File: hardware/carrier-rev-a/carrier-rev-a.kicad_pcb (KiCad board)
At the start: 2 copper layers, 250 x 210 mm, 107 parts, among them J1 SSQ-110-01-G-S, J10 SSQ-120-01-G-S, J11 SSQ-120-01-G-S, J2 SSQ-108-01-G-S, J3 SSQ-110-01-G-S, J4 SSQ-108-01-G-S, J5 SSQ-110-01-G-S, J6 SSQ-108-01-G-S, J7 SSQ-110-01-G-S, J8 SSQ-108-01-G-S, J9 5 V / 4 A INPUT, Q1 DMG2305UX-7, U2 TPS259470LRPWR, U3 AP2112K-3.3TRG1, U4 MCP23S17-E/SO, U5 SN74LVC8T245PWR, U6 SN74LVC8T245PWR, U7 SN74LVC1T45DBVR

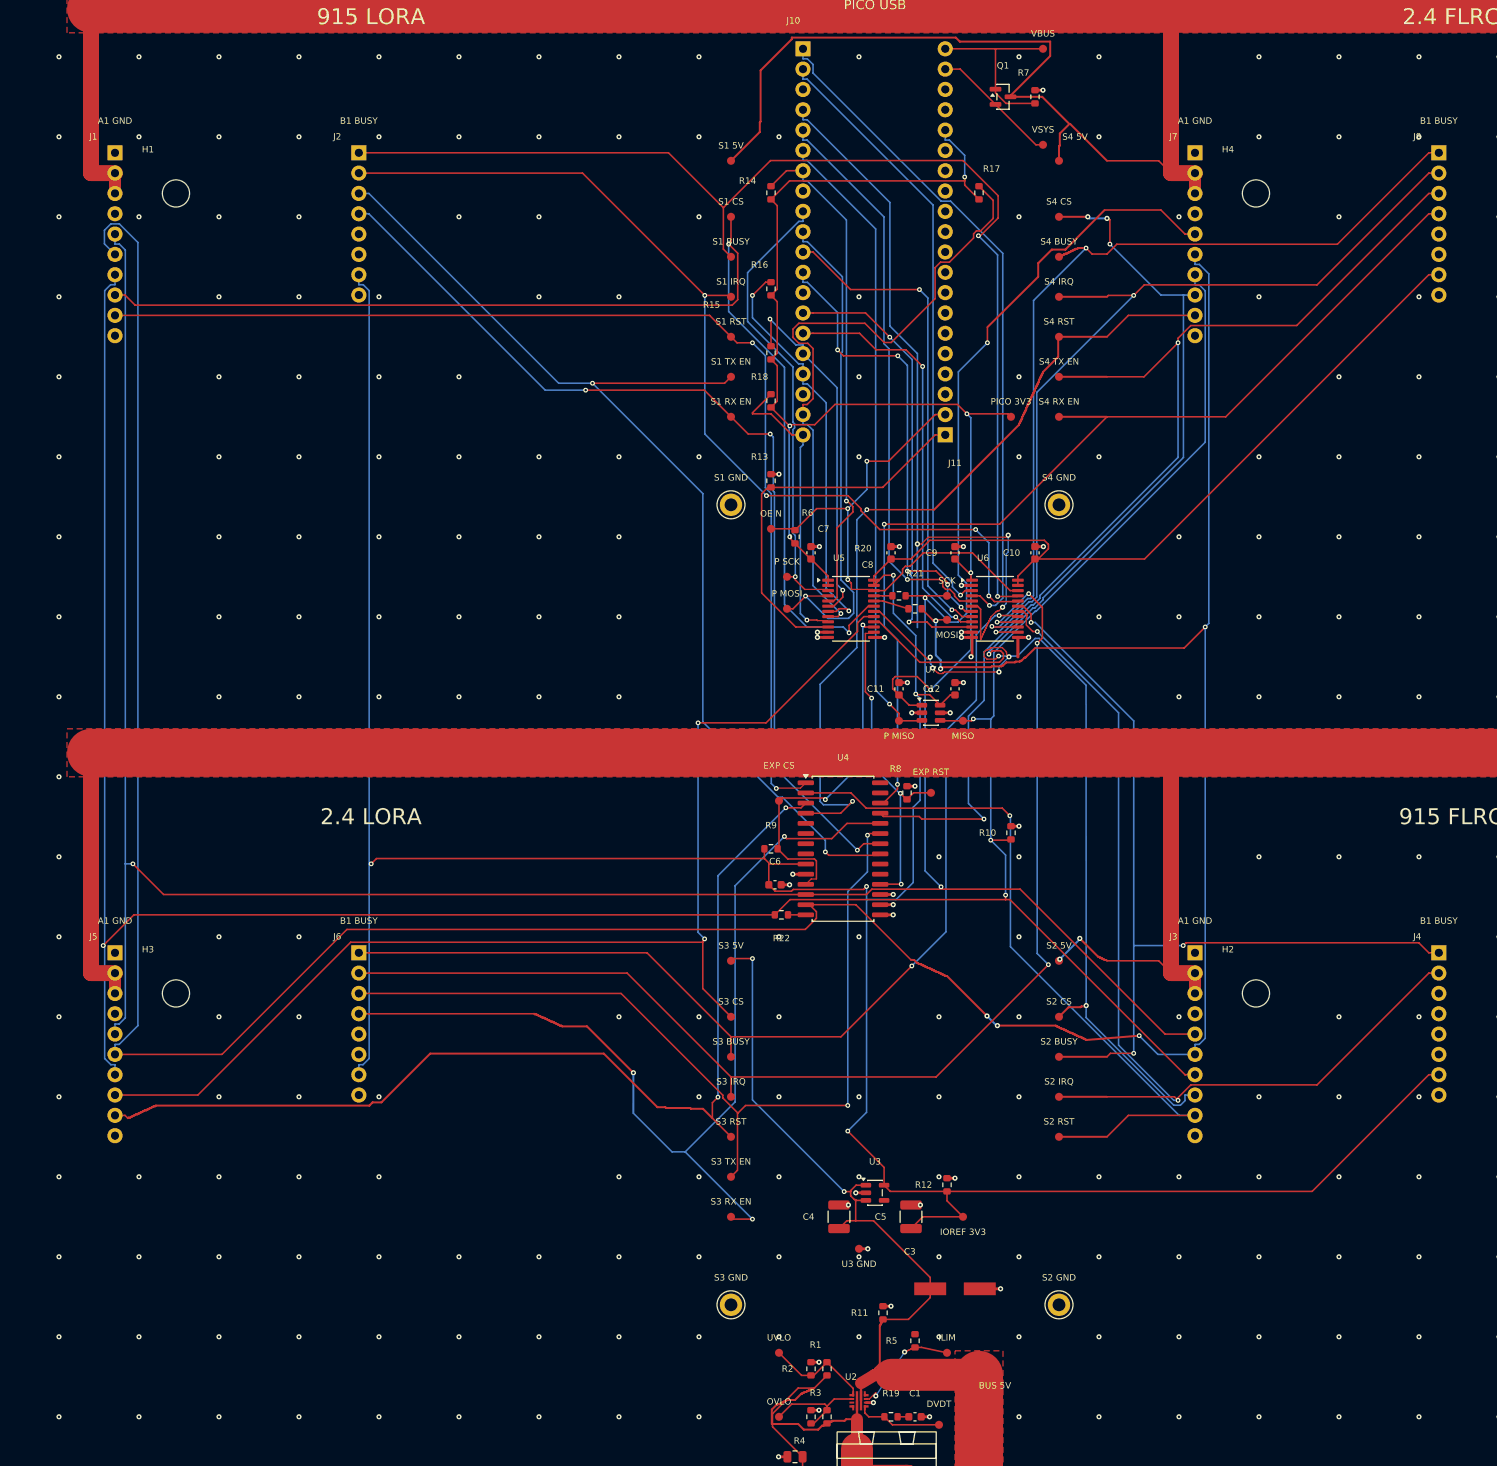
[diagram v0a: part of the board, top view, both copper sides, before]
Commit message: Improve Rev-A ground references and feedback routing
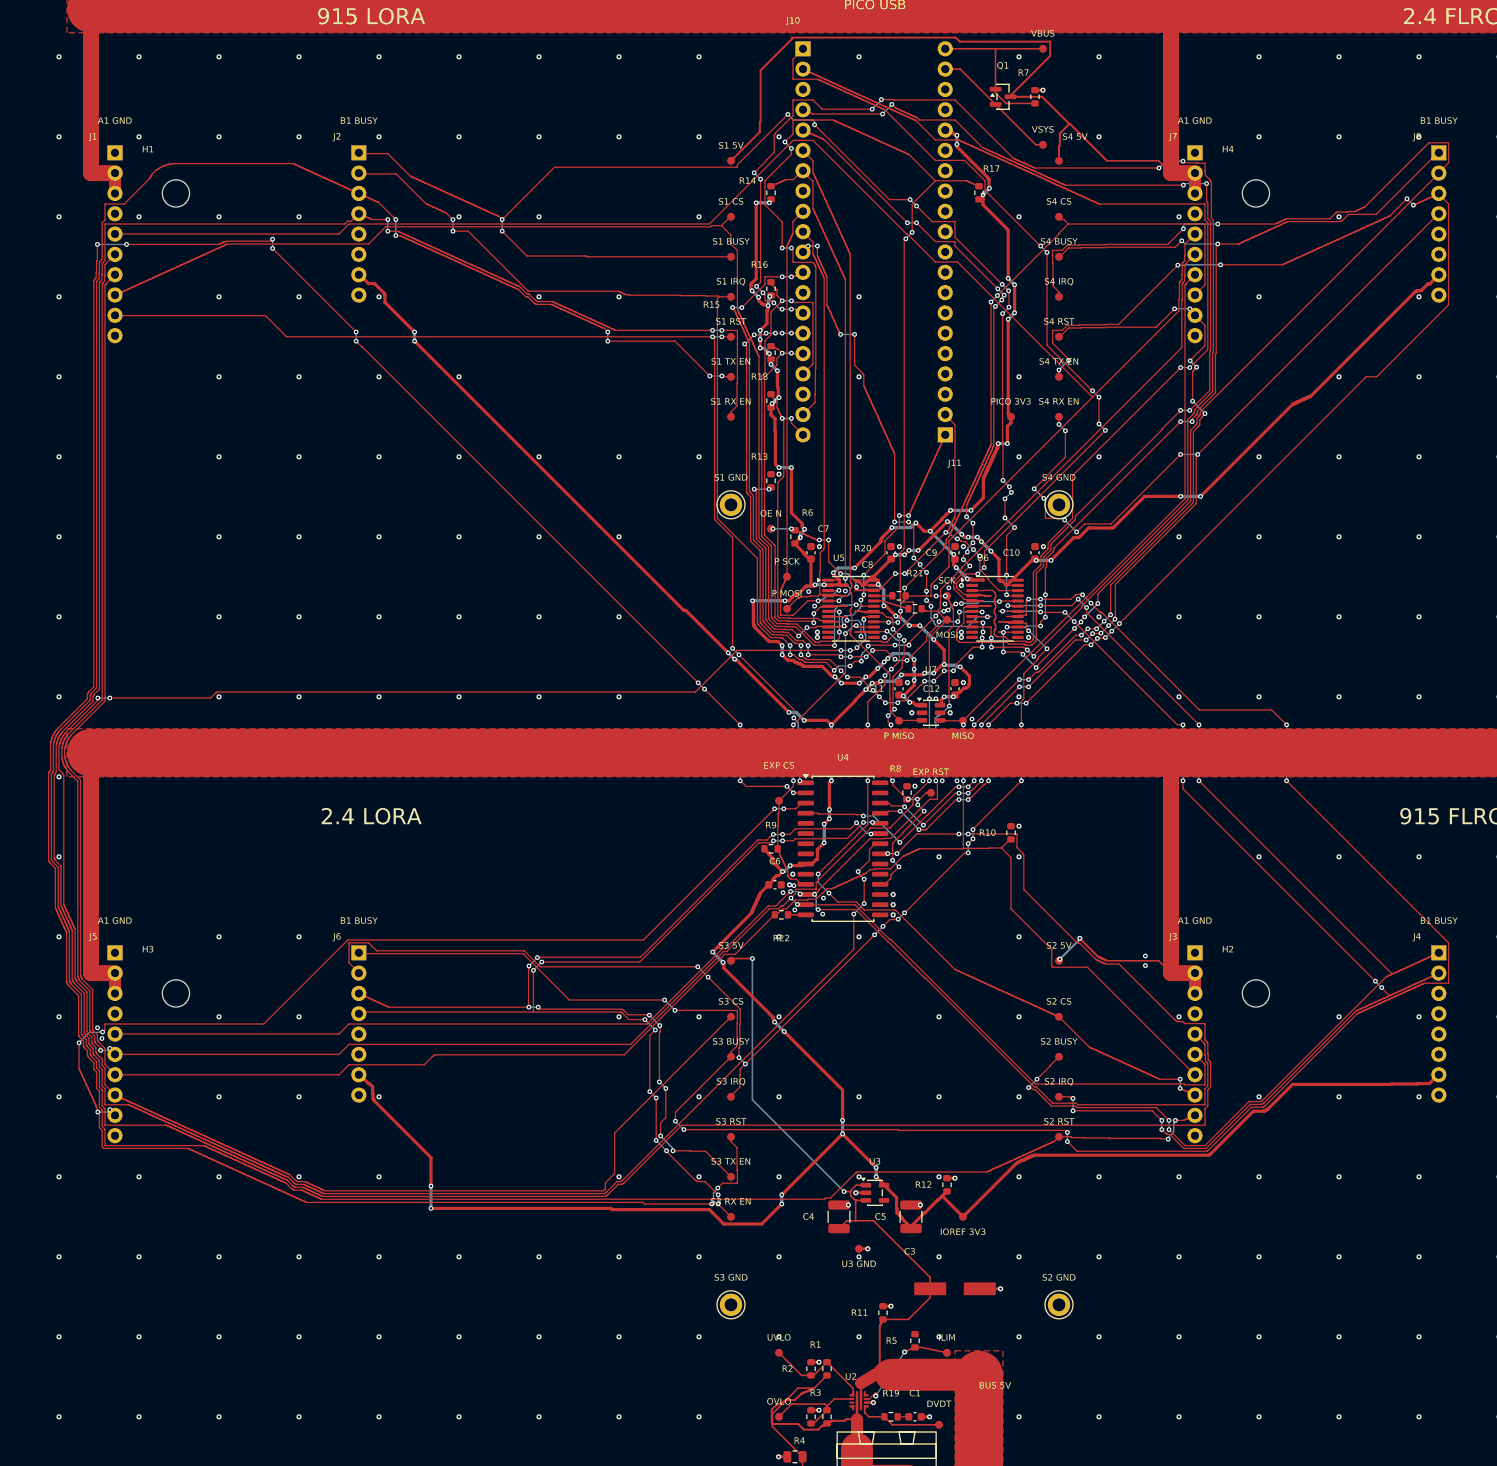
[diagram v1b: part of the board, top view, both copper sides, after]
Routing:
- net /S2_RESET_N: track 93.0 -> 385.5 mm, vias 1 -> 14
- net /S1_TX_EN: track 134.7 -> 427.2 mm, vias 2 -> 10
- net /S1_RX_EN: track 122.5 -> 339.4 mm, vias 3 -> 8
- net /S3_BUSY: track 130.7 -> 260.9 mm, vias 2 -> 12
- net /P_S4_IRQ: track 57.4 -> 172.5 mm, vias 2 -> 15
- net /S3_CS_N: track 148.1 -> 252.3 mm, vias 2 -> 6
- net /S3_RESET_N: track 130.1 -> 210.8 mm, vias 2 -> 8
- net /P_S4_CS_N: track 82.2 -> 143.5 mm, vias 1 -> 8
- net /P_S1_BUSY: track 75.9 -> 136.3 mm, vias 1 -> 2
- net /S4_IRQ: track 106.3 -> 158.7 mm, vias 2 -> 10
- net /SPI_SCK: track 366.3 -> 417.4 mm, vias 4 -> 8
- net /SPI_MOSI: track 413.6 -> 372.3 mm
- net /S4_TX_EN: track 141.9 -> 181.4 mm, vias 2 -> 19
- net /GND: track 49.6 -> 15.4 mm, vias 406 -> 426
- net /PICO_3V3: track 170.3 -> 203.8 mm, vias 6 -> 56
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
